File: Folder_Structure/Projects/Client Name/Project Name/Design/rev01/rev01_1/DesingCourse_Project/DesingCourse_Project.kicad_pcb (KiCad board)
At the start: 2 copper layers, 65 x 56 mm, 4 parts

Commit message: Update 16
Initial component placement done
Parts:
- added C1: 820u, LKMI2501K821MF:RA_LKMI2501K821MF_YMIN, B.Cu at (188.5, 137.0)
- added C10: 100n, Capacitor_SMD:C_0603_1608Metric, F.Cu at (153.7, 163.8)
- added C11: 100n, Capacitor_SMD:C_0603_1608Metric, F.Cu at (155.2, 163.8)
- added C12: 100n, Capacitor_SMD:C_0603_1608Metric, F.Cu at (158.2, 177.8)
- added C13: 100n, Capacitor_SMD:C_0603_1608Metric, F.Cu at (168.2, 175.8)
- added C14: 10p, Capacitor_SMD:C_0603_1608Metric, F.Cu at (147.2, 163.8)
- added C15: 10p, Capacitor_SMD:C_0603_1608Metric, F.Cu at (147.2, 171.8)
- added C16: 100n, Capacitor_SMD:C_0603_1608Metric, F.Cu at (168.2, 163.8)
- added C17: 100n, Capacitor_SMD:C_0603_1608Metric, F.Cu at (157.7, 162.2)
- added C18: 100n, Capacitor_SMD:C_0603_1608Metric, F.Cu at (154.2, 157.2)
- added C19: 2u2, Capacitor_SMD:C_0603_1608Metric, F.Cu at (166.2, 177.8)
- added C2: 820u, LKMI2501K821MF:RA_LKMI2501K821MF_YMIN, B.Cu at (198.0, 176.1)
- added C20: 2u2, Capacitor_SMD:C_0603_1608Metric, F.Cu at (170.2, 165.2)
- added C21: 100n, Capacitor_SMD:C_0603_1608Metric, F.Cu at (154.7, 171.8)
- added C22: 1u, Capacitor_SMD:C_0603_1608Metric, F.Cu at (153.2, 171.8)
- added C23: 100n, Capacitor_SMD:C_0603_1608Metric, F.Cu at (143.2, 134.7)
- added C24: 10n, Capacitor_SMD:C_0603_1608Metric, F.Cu at (273.6, 155.7)
- added C25: 2u2, Capacitor_SMD:C_0603_1608Metric, F.Cu at (273.6, 158.2)
- added C26: 2u2, Capacitor_SMD:C_0603_1608Metric, F.Cu at (273.6, 160.7)
- added C27: 120p, Capacitor_SMD:C_0603_1608Metric, F.Cu at (273.6, 163.2)
- added C28: 2u2, Capacitor_SMD:C_0603_1608Metric, F.Cu at (273.6, 165.7)
- added C29: 2u2, Capacitor_SMD:C_0603_1608Metric, F.Cu at (273.6, 168.2)
- added C3: 1u, Capacitor_SMD:C_0603_1608Metric, F.Cu at (165.6, 144.6)
- added C30: 22n, Capacitor_SMD:C_0603_1608Metric, F.Cu at (273.6, 170.7)
- added C31: 2u2, Capacitor_SMD:C_0603_1608Metric, F.Cu at (273.6, 173.2)
- added C32: 100n, Capacitor_SMD:C_0603_1608Metric, F.Cu at (277.6, 155.7)
- added C33: 100n, Capacitor_SMD:C_0603_1608Metric, F.Cu at (277.6, 158.2)
- added C34: 100n, Capacitor_SMD:C_0603_1608Metric, F.Cu at (277.6, 160.7)
- added C35: 100n, Capacitor_SMD:C_0603_1608Metric, F.Cu at (303.3, 157.2)
- added C36: 1u, Capacitor_SMD:C_0603_1608Metric, F.Cu at (277.6, 165.7)
- added C37: 1u, Capacitor_SMD:C_0603_1608Metric, F.Cu at (277.6, 168.2)
- added C38: 1u, Capacitor_SMD:C_0603_1608Metric, F.Cu at (277.6, 170.7)
- added C39: 10u, Capacitor_SMD:C_0603_1608Metric, F.Cu at (277.6, 173.2)
- added C4: 1u, Capacitor_SMD:C_0603_1608Metric, F.Cu at (167.1, 144.6)
- added C40: 1u, Capacitor_SMD:C_0603_1608Metric, F.Cu at (281.6, 155.7)
- added C41: 1u, Capacitor_SMD:C_0603_1608Metric, F.Cu at (281.6, 158.2)
- added C42: 10u, Capacitor_SMD:C_0603_1608Metric, F.Cu at (281.6, 160.7)
- added C43: 1u, Capacitor_SMD:C_0603_1608Metric, F.Cu at (281.6, 163.2)
- added C44: 10u, Capacitor_SMD:C_0603_1608Metric, F.Cu at (281.6, 165.7)
- added C45: 100n, Capacitor_SMD:C_0603_1608Metric, F.Cu at (281.6, 168.2)
- added C46: 100n, Capacitor_SMD:C_0603_1608Metric, F.Cu at (281.6, 170.7)
- added C47: 100n, Capacitor_SMD:C_0603_1608Metric, F.Cu at (281.6, 173.2)
- added C48: 2n2, Capacitor_SMD:C_0603_1608Metric, F.Cu at (189.5, 148.7)
- added C49: 2n2, Capacitor_SMD:C_0603_1608Metric, F.Cu at (189.5, 164.7)
- added C5: 1u, Capacitor_SMD:C_0603_1608Metric, F.Cu at (178.1, 142.1)
- added C50: 2u2, Capacitor_SMD:C_0603_1608Metric, F.Cu at (166.1, 149.2)
- added C51: 51p, Capacitor_SMD:C_0603_1608Metric, F.Cu at (144.1, 152.2)
- added C52: 51p, Capacitor_SMD:C_0603_1608Metric, F.Cu at (144.1, 146.2)
- added C53: 4n7, Capacitor_SMD:C_0603_1608Metric, F.Cu at (158.5, 186.5)
- added C54: 4n7, Capacitor_SMD:C_0603_1608Metric, F.Cu at (162.0, 186.5)
- added C55: 4n7, Capacitor_SMD:C_0603_1608Metric, F.Cu at (165.5, 186.5)
- added C56: 100n, Capacitor_SMD:C_0603_1608Metric, F.Cu at (157.5, 182.5)
- added C57: 100n, Capacitor_SMD:C_0603_1608Metric, F.Cu at (161.0, 182.5)
- added C58: 100n, Capacitor_SMD:C_0603_1608Metric, F.Cu at (166.5, 182.5)
- added C59: 4n7, Capacitor_SMD:C_0603_1608Metric, F.Cu at (154.5, 186.5)
- added C6: 1u, Capacitor_SMD:C_0603_1608Metric, F.Cu at (179.6, 142.1)
- added C60: 100n, Capacitor_SMD:C_0603_1608Metric, F.Cu at (153.5, 182.5)
- added C7: 100n, Capacitor_SMD:C_0603_1608Metric, F.Cu at (212.7, 140.8)
- added C8: 100n, Capacitor_SMD:C_0603_1608Metric, F.Cu at (146.5, 183.6)
- added C9: 10u, Capacitor_SMD:C_0603_1608Metric, F.Cu at (152.2, 163.8)
- added D1: SMAJ60CA, Diode_SMD:D_SMA, F.Cu at (209.2, 137.8)
- added D10: LED_G, Diode_SMD:D_1206_3216Metric, F.Cu at (170.7, 185.2)
- added D11: LED_R, Diode_SMD:D_1206_3216Metric, F.Cu at (173.2, 185.2)
- added D12: BAT60A, Diode_SMD:D_SOD-323, F.Cu at (162.5, 135.4)
- added D13: PMEG6020AELR, Diode_SMD:Nexperia_CFP3_SOD-123W, F.Cu at (274.4, 176.1)
- added D14: BAT60A, Diode_SMD:D_SOD-323, F.Cu at (279.4, 176.0)
- added D15: ESDCAN24-2BLY, ESDCAN24-2BLY:SOT95P237X112-3N, F.Cu at (138.1, 149.2)
- added D2: LED_G, Diode_SMD:D_1206_3216Metric, F.Cu at (215.2, 132.8)
- added D3: LED_G, Diode_SMD:D_1206_3216Metric, F.Cu at (162.1, 142.1)
- added D4: BAT60A, Diode_SMD:D_SOD-323, F.Cu at (182.0, 142.9)
- added D5: LED_G, Diode_SMD:D_1206_3216Metric, F.Cu at (183.1, 139.1)
- added D6: PESD3V3U1UA,115, PESD3V3U1UA_115:DIO_PESD3V3U1UA_115, F.Cu at (137.6, 164.5)
- added D7: BAT60A, Diode_SMD:D_SOD-323, F.Cu at (141.6, 164.5)
- added D8: SMAJ5.0A, Diode_SMD:D_SMA, F.Cu at (137.6, 159.5)
- added D9: BAT60A, Diode_SMD:D_SOD-323, F.Cu at (141.6, 161.5)
- added FB1: 120R, BLM18PG121SN1D:BEADC1608X95N, F.Cu at (151.7, 171.8)
- added FID1: 1mm/circular, Fiducial:Fiducial_1mm_Mask2mm, F.Cu at (130.0, 133.2)
- added FID2: 1mm/circular, Fiducial:Fiducial_1mm_Mask2mm, F.Cu at (220.0, 133.2)
- added FID3: 1mm/circular, Fiducial:Fiducial_1mm_Mask2mm, F.Cu at (220.0, 188.2)
- added ID1: ~, JGB_Library:hot-surface, F.Cu at (341.3, 68.6)
- added ID2: ~, JGB_Library:high-voltage, F.Cu at (323.8, 83.9)
- added ID3: ~, JGB_Library:ESD-suceptible, F.Cu at (326.1, 69.3)
- added ID4: ~, JGB_Library:IC-logo, F.Cu at (352.8, 80.9)
- added ID5: ~, JGB_Library:4_Layer_ID, F.Cu at (198.2, 197.6)
- added ID6: ~, JGB_Library:Project_ID, F.Cu at (334.4, 98.3)
- added J1: XT60PW-M, XT60PW-M:AMASS_XT60PW-M, F.Cu at (199.0, 134.2)
- added J10: 874380443, 874380843:MOLEX_874380443, F.Cu at (130.1, 149.2)
- added J11: 874380643, 874380843:MOLEX_874380643, F.Cu at (160.5, 193.0)
- added J2: TYPE-C-31-M-12, TYPE-C-31-M-12:HRO_TYPE-C-31-M-12, F.Cu at (178.4, 125.3)
- added J3: 874380243, 874380843:MOLEX_874380243, F.Cu at (146.7, 193.2)
- added J4: 874380843, 874380843:MOLEX_874380843, F.Cu at (130.1, 168.0)
- added J5: 874380343, 874380843:MOLEX_874380343, F.Cu at (143.2, 128.2)
- added J6: 874380643, 874380843:MOLEX_874380643, F.Cu at (157.5, 128.4)
- added J7: 7461084, WP-BUTR:WP-BUTR_7461084, F.Cu at (218.8, 149.2)
- added J8: 7461084, WP-BUTR:WP-BUTR_7461084, F.Cu at (218.8, 165.2)
- added J9: 7461084, WP-BUTR:WP-BUTR_7461084, F.Cu at (218.8, 181.2)
- added L1: 22u, L_Bourns_SDR0805:IND_BOURNS_SDR0805, F.Cu at (298.3, 148.8)
- added L2: 744227S, WE-SL2:WE-SL2, F.Cu at (151.1, 149.2)
- added NT1: NetTie_2, NetTie:NetTie-2_SMD_Pad0.5mm, F.Cu at (278.5, 178.2)
- added NT2: NetTie_2, NetTie:NetTie-2_SMD_Pad0.5mm, F.Cu at (210.8, 149.7)
- added NT3: NetTie_2, NetTie:NetTie-2_SMD_Pad0.5mm, F.Cu at (210.8, 165.7)
- added NT4: NetTie_2, NetTie:NetTie-2_SMD_Pad0.5mm, F.Cu at (210.8, 181.7)
- added NT5: NetTie_2, NetTie:NetTie-2_SMD_Pad0.5mm, F.Cu at (203.3, 183.2)
- added Q1: HSBA15810C, Package_SO:HSBA15810C, F.Cu at (208.8, 146.2)
- added Q2: HSBA15810C, Package_SO:HSBA15810C, F.Cu at (208.8, 153.2)
- added Q3: HSBA15810C, Package_SO:HSBA15810C, F.Cu at (208.8, 162.2)
- added Q4: HSBA15810C, Package_SO:HSBA15810C, F.Cu at (208.8, 169.2)
- added Q5: HSBA15810C, Package_SO:HSBA15810C, F.Cu at (208.8, 178.2)
- added Q6: HSBA15810C, Package_SO:HSBA15810C, F.Cu at (208.8, 185.1)
- added R1: 39k, Resistor_SMD:R_0603_1608Metric, F.Cu at (211.2, 132.8)
- added R10: 1k, Resistor_SMD:R_0603_1608Metric, F.Cu at (184.6, 142.1)
- added R11: 39k, Resistor_SMD:R_0603_1608Metric, F.Cu at (212.7, 137.4)
- added R12: 2k2, Resistor_SMD:R_0603_1608Metric, F.Cu at (214.2, 140.8)
- added R13: 2k2, Resistor_SMD:R_0603_1608Metric, F.Cu at (146.5, 185.1)
- added R14: 2k2, Resistor_SMD:R_0603_1608Metric, F.Cu at (144.2, 157.2)
- added R15: 0R, Resistor_SMD:R_0603_1608Metric, F.Cu at (151.7, 166.8)
- added R16: 0R, Resistor_SMD:R_0603_1608Metric, F.Cu at (151.7, 169.3)
- added R17: 1k, Resistor_SMD:R_0603_1608Metric, F.Cu at (170.7, 181.2)
- added R18: 1k, Resistor_SMD:R_0603_1608Metric, F.Cu at (173.2, 181.2)
- added R19: 0R, Resistor_SMD:R_0603_1608Metric, F.Cu at (160.7, 160.8)
- added R2: 0R, Resistor_SMD:R_0603_1608Metric, F.Cu at (173.9, 132.8)
- added R20: 2k2, Resistor_SMD:R_0603_1608Metric, F.Cu at (141.7, 134.7)
- added R21: 16k, Resistor_SMD:R_0603_1608Metric, F.Cu at (285.7, 155.7)
- added R22: 205k, Resistor_SMD:R_0603_1608Metric, F.Cu at (285.7, 158.2)
- added R23: 10k, Resistor_SMD:R_0603_1608Metric, F.Cu at (285.7, 160.7)
- added R24: 10k, Resistor_SMD:R_0603_1608Metric, F.Cu at (285.7, 163.2)
- added R25: 1M, Resistor_SMD:R_0603_1608Metric, F.Cu at (285.7, 165.7)
- added R26: 18k, Resistor_SMD:R_0603_1608Metric, F.Cu at (285.7, 168.2)
- added R27: 3k3, Resistor_SMD:R_0603_1608Metric, F.Cu at (285.7, 170.7)
- added R28: 39k, Resistor_SMD:R_0603_1608Metric, F.Cu at (285.7, 173.2)
- added R29: 2k2, Resistor_SMD:R_0603_1608Metric, F.Cu at (289.7, 155.7)
- added R3: 0R, Resistor_SMD:R_0603_1608Metric, F.Cu at (172.4, 132.8)
- added R30: 39k, Resistor_SMD:R_0603_1608Metric, F.Cu at (289.7, 158.2)
- added R31: 2k2, Resistor_SMD:R_0603_1608Metric, F.Cu at (289.7, 160.7)
- added R32: 39k, Resistor_SMD:R_0603_1608Metric, F.Cu at (289.7, 163.2)
- added R33: 2k2, Resistor_SMD:R_0603_1608Metric, F.Cu at (289.7, 165.7)
- added R34: 4R7, Resistor_SMD:R_0603_1608Metric, F.Cu at (210.1, 142.5)
- added R35: 4R7, Resistor_SMD:R_0603_1608Metric, F.Cu at (202.8, 154.2)
- added R36: 39k, Resistor_SMD:R_0603_1608Metric, F.Cu at (204.3, 154.2)
- added R37: 100R, Resistor_SMD:R_0603_1608Metric, F.Cu at (191.8, 149.4)
- added R38: 100R, Resistor_SMD:R_0603_1608Metric, F.Cu at (191.8, 147.9)
- added R39: 1m, RES_WSLP2726L5000FEA:WSLP2726_1mOHM_VIS, F.Cu at (197.8, 148.7)
- added R4: 0R, Resistor_SMD:R_0603_1608Metric, F.Cu at (175.5, 135.8)
- added R40: 4R7, Resistor_SMD:R_0603_1608Metric, F.Cu at (210.8, 158.2)
- added R41: 4R7, Resistor_SMD:R_0603_1608Metric, F.Cu at (202.8, 170.2)
- added R42: 39k, Resistor_SMD:R_0603_1608Metric, F.Cu at (204.3, 170.2)
- added R43: 100R, Resistor_SMD:R_0603_1608Metric, F.Cu at (191.8, 165.4)
- added R44: 100R, Resistor_SMD:R_0603_1608Metric, F.Cu at (191.8, 163.9)
- added R45: 1m, RES_WSLP2726L5000FEA:WSLP2726_1mOHM_VIS, F.Cu at (197.8, 164.7)
- added R46: 4R7, Resistor_SMD:R_0603_1608Metric, F.Cu at (210.8, 174.2)
- added R47: 4R7, Resistor_SMD:R_0603_1608Metric, F.Cu at (202.8, 186.2)
- added R48: 39k, Resistor_SMD:R_0603_1608Metric, F.Cu at (204.3, 186.2)
- added R49: 10k, Resistor_SMD:R_0603_1608Metric, F.Cu at (159.6, 152.8)
- added R5: 5k1, Resistor_SMD:R_0603_1608Metric, F.Cu at (178.5, 135.8)
- added R50: 10R, Resistor_SMD:R_0603_1608Metric, F.Cu at (144.1, 147.8)
- added R51: 10R, Resistor_SMD:R_0603_1608Metric, F.Cu at (144.1, 150.8)
- added R52: 120R, Resistor_SMD:R_0603_1608Metric, F.Cu at (141.6, 149.2)
- added R53: 2k2, Resistor_SMD:R_0603_1608Metric, F.Cu at (158.5, 185.0)
- added R54: 2k2, Resistor_SMD:R_0603_1608Metric, F.Cu at (162.0, 185.0)
- added R55: 2k2, Resistor_SMD:R_0603_1608Metric, F.Cu at (165.5, 185.0)
- added R56: 10k, Resistor_SMD:R_0603_1608Metric, F.Cu at (159.0, 182.5)
- added R57: 10k, Resistor_SMD:R_0603_1608Metric, F.Cu at (162.5, 182.5)
- added R58: 10k, Resistor_SMD:R_0603_1608Metric, F.Cu at (165.0, 182.5)
- added R59: 10k, Resistor_SMD:R_0603_1608Metric, F.Cu at (154.5, 185.0)
- added R6: 5k1, Resistor_SMD:R_0603_1608Metric, F.Cu at (177.0, 135.8)
- added R60: 0R, Resistor_SMD:R_0603_1608Metric, F.Cu at (155.0, 182.5)
- added R61: 0R, Resistor_SMD:R_0603_1608Metric, F.Cu at (136.1, 128.5)
- added R62: 0R, Resistor_SMD:R_0603_1608Metric, F.Cu at (215.0, 128.2)
- added R63: 0R, Resistor_SMD:R_0603_1608Metric, F.Cu at (212.5, 193.8)
- added R64: 0R, Resistor_SMD:R_0603_1608Metric, F.Cu at (137.5, 193.2)
- added R7: 22R, Resistor_SMD:R_0603_1608Metric, F.Cu at (181.0, 135.8)
- added R8: 22R, Resistor_SMD:R_0603_1608Metric, F.Cu at (182.5, 135.8)
- added R9: 1k, Resistor_SMD:R_0603_1608Metric, F.Cu at (163.1, 145.4)
- added SW1: ~, PTS526SK15SMTR2LFS:SMT_FS, F.Cu at (149.2, 157.2)
- added TH1: 10k, Resistor_SMD:R_0603_1608Metric, F.Cu at (146.5, 187.1)
- added U1: PUSB3AB6Z, PUSB3AB6Z:IC_PUSB3AB6Z, F.Cu at (178.0, 132.8)
- added U2: AMS1117-3.3, Package_TO_SOT_SMD:SOT-223-3_TabPin2, F.Cu at (172.2, 143.0)
- added U3: STM32F405RGTx, Package_QFP:LQFP-64_10x10mm_P0.5mm, F.Cu at (162.2, 169.8)
- added U4: DRV8302DCA, DRV8302DCA:SOP50P810X120-57N, F.Cu at (297.3, 162.2)
- added U5: SN65HVD230D, SN65HVD230D:SOIC127P599X175-8N, F.Cu at (161.6, 149.2)
- added Y1: 8MHz, X50328MSB2GI:XTAL_MSB2GI_YXC, F.Cu at (148.2, 167.8)
- MH1, MH2, MH3, MH4: value MountingHole_2.7mm_M2.5 -> M3; footprint MountingHole:MountingHole_2.7mm_M2.5 -> MountingHole:MountingHole_3mm_Pad_Via
- moved MH3 57.8 mm to (130.0, 193.2)
- moved MH1 55.5 mm to (130.0, 128.2)
- moved MH4 27.9 mm to (220.0, 193.2)
- moved MH2 24.1 mm to (220.0, 128.2)
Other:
- board size 65 x 56 mm -> 100 x 75 mm
- copper layers 2 -> 4
- board text added: "CAN"
- board text added: "COM"
- board text added: "FILTERS"
- board text added: "INPUT"
- board text added: "OUTPUT"
- board text added: "PROG"
- board text added: "SENSOR"
- board text added: "SERVO"
- board text added: "USB"
- board text removed: "Extend PCB edge 0.5mm if using SMT header"

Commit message: Update17
Design rules and stack defined.

Check againg DR and proceed with layout.
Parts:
- C39, C42, C44: footprint Capacitor_SMD:C_0603_1608Metric -> Capacitor_SMD:C_1210_3225Metric
- C45, C46, C47, C48, C49, R37, R38, R43, R44: moved to B.Cu
- moved R26 113.7 mm to (172.1, 162.7), turned to -90 degrees
- moved U4 113.7 mm to (184.2, 173.4)
- moved L1 113.3 mm to (185.4, 158.4), turned to 180 degrees
- moved C35 112.9 mm to (190.9, 167.9)
- moved R27 112.3 mm to (173.6, 162.7), turned to 90 degrees
- moved D14 110.6 mm to (170.1, 158.9), turned to -90 degrees
- moved R21 110.0 mm to (176.4, 168.2)
- moved R23 109.7 mm to (176.4, 169.9)
- moved R24 109.6 mm to (176.4, 171.7)
- moved R22 109.5 mm to (176.4, 164.9)
- moved C44 109.0 mm to (172.9, 158.4), turned to 90 degrees
- moved C42 105.5 mm to (176.1, 158.4), turned to 90 degrees
- moved NT1 104.5 mm to (174.0, 174.9)
- moved R62 103.1 mm to (135.0, 193.2), turned to 0 degrees
- moved C40 101.4 mm to (180.6, 164.4), turned to 90 degrees
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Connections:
- net Net-(C24-Pad1) renamed /MOSFET_DRIVER/Node8
- net Net-(D10-A) renamed /MCU/Node5
- net Net-(D11-A) renamed /MCU/Node6
- net Net-(D2-A) renamed /INPUT/Node1
- net Net-(D3-A) renamed /STEP_DOWN/Node2
- net Net-(D5-A) renamed /STEP_DOWN/Node3
- net Net-(J2-SHIELD-PadS1) renamed /USB-C/Shield_USB
- net Net-(J5-3-Pad3_1) renamed /MCU/Node7
- net Net-(MH1-Pad1) renamed /MECHANICAL/Node10
- net Net-(MH2-Pad1) renamed /MECHANICAL/Node11
- net Net-(MH3-Pad1) renamed /MECHANICAL/Node12
- net Net-(MH4-Pad1) renamed /MECHANICAL/Node13
- net Net-(R14-Pad1) renamed /MCU/Node4
- net Net-(U4-AVDD) renamed /MOSFET_DRIVER/<NO NET>
- net Net-(U5-RS) renamed /CAN/CAN_RS
- D15 pad 1: /CAN/CONN_CAN_P -> /CAN/CONN_CAN_N
- D15 pad 2: /CAN/CONN_CAN_N -> /CAN/CONN_CAN_P
- J10 pad 1_1: P5V -> GND
- J10 pad 1_2: P5V -> GND
- J10 pad 2_1: /CAN/CONN_CAN_P -> /CAN/CONN_CAN_N
- J10 pad 2_2: /CAN/CONN_CAN_P -> /CAN/CONN_CAN_N
- J10 pad 3_1: /CAN/CONN_CAN_N -> /CAN/CONN_CAN_P
- J10 pad 3_2: /CAN/CONN_CAN_N -> /CAN/CONN_CAN_P
- J10 pad 4_1: GND -> P5V
- J10 pad 4_2: GND -> P5V
- L2 pad 1: /CAN/R_CAN_P -> /CAN/R_CAN_N
- L2 pad 2: /CAN/R_CAN_N -> /CAN/R_CAN_P
- L2 pad 3: /CAN/CAN_N -> /CAN/CAN_P
- L2 pad 4: /CAN/CAN_P -> /CAN/CAN_N
- U1 pad 3: /USB-C/P5V-C -> VBUS
- U1 pad 5: /USB-C/P5V-C -> VBUS
- U3 pad 14: SENS3 -> SENS1
- U3 pad 16: SENS1 -> SENS3

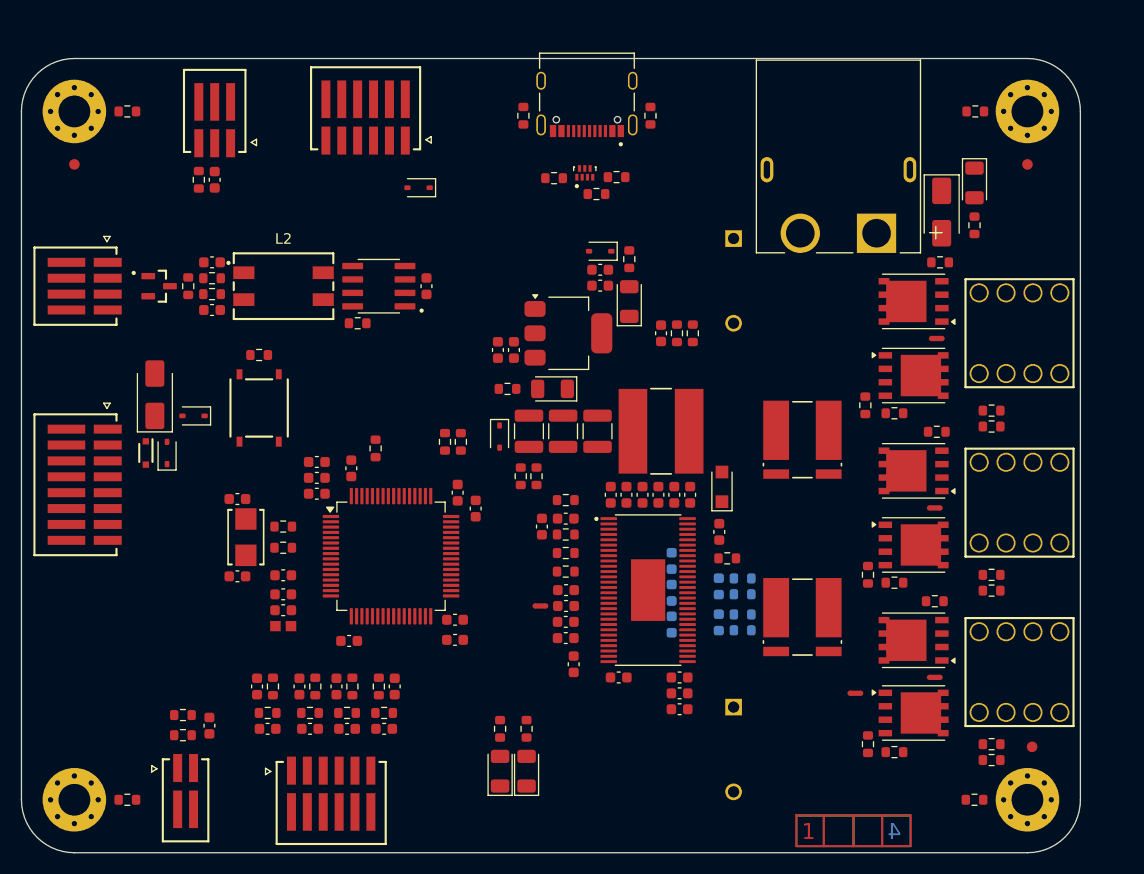
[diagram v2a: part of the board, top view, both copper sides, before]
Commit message: Update18
Layout finished, clean up or layout and designators.
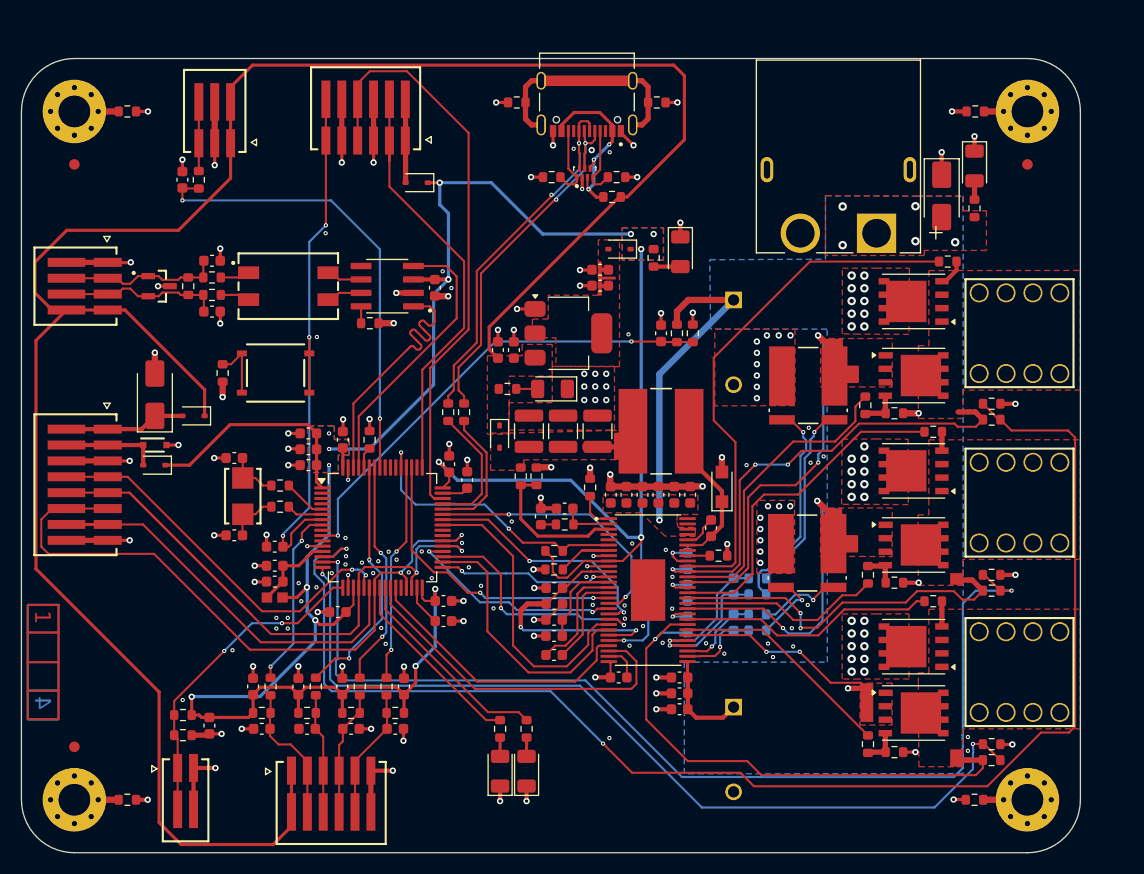
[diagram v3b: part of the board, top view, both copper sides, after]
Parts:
- moved FID3 90.4 mm to (130.0, 188.2)
- moved ID5 76.1 mm to (125.6, 174.8), turned to -90 degrees
- moved NT4 8.31 mm to (214.1, 189.5), turned to 180 degrees
- moved NT2 7.38 mm to (213.9, 156.6), turned to 180 degrees
- moved NT3 7.32 mm to (213.9, 172.5), turned to 180 degrees
- moved D5 6.74 mm to (187.2, 141.5), turned to -90 degrees
- moved R45 6.07 mm to (199.2, 169.9)
- moved C1 5.80 mm to (192.2, 146.0)
- moved R39 5.15 mm to (199.3, 154.1)
- moved C14 3.89 mm to (145.1, 161.0)
- moved C15 3.89 mm to (145.1, 168.3)
- moved R15 3.89 mm to (149.4, 163.6)
- moved R16 3.89 mm to (149.4, 165.6)
- moved Y1 3.89 mm to (145.9, 164.6)
- moved R14 3.84 mm to (144.0, 152.9), turned to -90 degrees
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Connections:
- net /MOSFET_DRIVER/<NO NET> renamed /MOSFET_DRIVER/Node9
- net Net-(D4-A) renamed /STEP_DOWN/P3V3_I
- R56 pad 2: HALL1_OUT -> HALL_1_OUT
- R57 pad 2: HALL2_OUT -> HALL_2_OUT
- R58 pad 2: HALL3_OUT -> HALL_3_OUT
- U3 pad 26: BR_SD2 -> BR_SO2
- U3 pad 27: BR_SD1 -> BR_SO1
- U3 pad 52: /MCU/HALL3_OUT -> HALL_3_OUT
- U3 pad 58: /MCU/HALL1_OUT -> HALL_2_OUT
- U3 pad 59: /MCU/HALL2_OUT -> HALL_1_OUT
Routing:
- net P3V3: track 0.00 -> 244.9 mm, vias 0 -> 16
- net P5V: track 0.00 -> 208.5 mm
- net GND: track 0.00 -> 164.3 mm, vias 0 -> 178
- net SENS1: track 0.00 -> 132.7 mm, vias 0 -> 2
- net SENS2: track 0.00 -> 99.7 mm, vias 0 -> 2
- net SENS3: track 0.00 -> 83.8 mm, vias 0 -> 2
- net /MCU/RX_SDA_NSS: track 0.00 -> 71.2 mm, vias 0 -> 2
- net /MCU/TX_SCL_MOSI: track 0.00 -> 64.8 mm, vias 0 -> 2
- net /MCU/SWDIO: track 0.00 -> 55.8 mm
- net /MCU/NRST: track 0.00 -> 54.6 mm, vias 0 -> 3
- net H3_VS: track 0.00 -> 51.6 mm, vias 0 -> 1
- net M_H1: track 0.00 -> 49.9 mm
- net /MCU/AN_IN: track 0.00 -> 44.6 mm, vias 0 -> 2
- net /MCU/SERVO: track 0.00 -> 43.9 mm, vias 0 -> 2
- net H1_VS: track 0.00 -> 43.3 mm, vias 0 -> 3
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- added copper zone on B.Cu, net +VDC
- added copper zone on F.Cu, net +VDC
- added copper zone on F.Cu, net /MOSFET/PHASE_1
- added copper zone on F.Cu, net /MOSFET/PHASE_2
- added copper zone on F.Cu, net /MOSFET/PHASE_3
- added copper zone on F.Cu, net /MOSFET_DRIVER/P5V_DRV
- added copper zone on F.Cu, net /STEP_DOWN/P3V3_I
- added copper zone on F.Cu, net GND
- added copper zone on In1.Cu, net GND
- added copper zone on In2.Cu, net GND
- added copper zone on F.Cu, net H1_LOW
- added copper zone on F.Cu, net H2_LOW
- added copper zone on F.Cu, net H3_LOW
- added copper zone on B.Cu, net P3V3
- added copper zone on F.Cu, net P3V3
- added copper zone on F.Cu, net P5V

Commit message: Update19
PCB finished before applying curved traces
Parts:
- C14, ID4, ID6: moved to B.Cu
- moved ID4 206.0 mm to (153.0, 130.8), turned to 180 degrees
- moved ID3 188.8 mm to (181.2, 190.3)
- moved ID6 181.8 mm to (160.0, 149.7), turned to 180 degrees
- moved ID2 144.4 mm to (188.4, 134.2)
- moved ID1 143.1 mm to (200.0, 190.4)
- moved D10 2.58 mm to (167.6, 190.5)
- moved D11 2.58 mm to (170.1, 190.5)
- moved R17 2.58 mm to (167.6, 186.5)
- moved R18 2.58 mm to (170.1, 186.5)
- moved C23 1.93 mm to (138.2, 134.7)
- moved R20 1.93 mm to (139.8, 134.7)
- moved R4 0.05 mm to (180.7, 136.3)
- moved R5 0.05 mm to (181.1, 134.4)
- moved R6 0.05 mm to (175.0, 134.4)
- moved U1 0.05 mm to (178.1, 134.1)
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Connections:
- net CAN_RX renamed CAN_TXRX_N
- net CAN_TX renamed CAN_TXRX_P
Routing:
- net /USB-C/USB-C_N: track 35.5 -> 38.5 mm
- net /MCU/LED_RED: track 19.7 -> 17.1 mm
- net H1: track 25.4 -> 23.3 mm
- net /MCU/SERVO: track 43.9 -> 45.8 mm
- net /MCU/LED_GREEN: track 18.0 -> 16.1 mm
- net /MCU/Node7: track 6.53 -> 7.80 mm
- net /USB-C/USB-C_P: track 37.1 -> 37.8 mm
- net /USB-C/CC2: track 7.05 -> 7.58 mm
- net GND: vias 178 -> 185
- added copper zone on B.Cu, net GND
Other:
- board text added: "*"
- board text added: "+VDC"
- board text added: "+VDC - ON"
- board text added: "0.03 mm"
- board text added: "0.07 mm"
- board text added: "0.1200 mm / 0.2000 mm"
- board text added: "0.203 mm"
- board text added: "1.03 mm"
- board text added: "1.6560 mm"
- board text added: "100.0000 mm x 75.0000 mm"
- board text added: "4"
- board text added: "4.6"
- board text added: "BOT_SGN.Cu"
- board text added: "Blue"
- board text added: "COMM"
- board text added: "D15"
- board text added: "D6"
- board text added: "Dielectric 1"
- board text added: "Dielectric 2"
- board text added: "Dielectric 3"
- board text added: "FB1"
- board text added: "GND"
- board text added: "GND CAN_N CAN_P P5V"
- board text added: "GREEN LED"
- board text added: "H1"
- board text added: "H2"
- board text added: "H3"
- board text added: "HAL lead-free"
- board text added: "J1"
- board text added: "J10"
- board text added: "J11"
- board text added: "J2"
- board text added: "J3"
- board text added: "J4"
- board text added: "J5"
- board text added: "J6"
- board text added: "J7"
- board text added: "J8"
- board text added: "J9"
- board text added: "L2"
- board text added: "L2_GND.Cu"
- board text added: "L3_GND.Cu"
- board text added: "NRST GND SWDIO GND SWCLK P3V3"
- board text added: "P3V3 - ON"
- board text added: "P5V"
- board text added: "P5V - ON"
- board text added: "P5V P3V3 GND SCK_ADC_EXT RX_SDA_NSS TX_SCL_MOSI MISO_ADC_EXT2 GND"
- board text added: "RED LED"
- board text added: "T1"
- board text added: "TEMP & HALL SENSOR"
- board text added: "THERMISTOR"
- board text added: "TOP_SGN.Cu"
- board text added: "U1"
- board text added: "U4"
- board text added: "U5"
- board text added: "USB-C"
- board text added: "White"
- board text added: "Yes"
- board text added: "prepreg"
- board text removed: "0.035 mm"
- board text removed: "0.2000 mm / 0.0000 mm"
- board text removed: "1.51 mm"
- board text removed: "1.6000 mm"
- board text removed: "2"
- board text removed: "4.5"
- board text removed: "65.1000 mm x 56.1000 mm"
- board text removed: "B.Cu"
- board text removed: "Dielectric"
- board text removed: "F.Cu"
- board text removed: "Green"
- board text removed: "None"

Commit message: Update20
DRC "clear".

Create gerber files
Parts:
- C14: moved to F.Cu
- moved D1 0.72 mm to (211.9, 135.5)
- moved NT5 0.50 mm to (204.2, 183.2)
- turned C14 to 180 degrees
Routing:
- net /MCU/RX_SDA_NSS: track 71.2 -> 54.4 mm
- net /MCU/SWCLK: track 41.3 -> 38.3 mm
- net GND: track 164.3 -> 167.2 mm, vias 185 -> 524
- net /MOSFET_DRIVER/DTC: track 7.54 -> 5.10 mm
- net /MOSFET/SH1_P: track 21.1 -> 19.0 mm
- net H2_VS: track 33.8 -> 35.9 mm, vias 2 -> 3
- net SENS1: track 132.7 -> 130.7 mm
- net P5V: track 208.5 -> 206.7 mm
- net P3V3: track 244.9 -> 243.1 mm
- net H3_VS: track 51.6 -> 50.0 mm
- net /MCU/TX_SCL_MOSI: track 64.8 -> 63.1 mm
- net SENS3: track 83.8 -> 82.6 mm
- net H1_VS: track 43.3 -> 42.2 mm
- net H3: track 28.5 -> 27.4 mm
- net /MCU/SWDIO: track 55.9 -> 54.8 mm
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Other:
- board text added: "0.2000 mm"
- board text added: "BOTTOM ASSEMBLY"
- board text added: "TOP ASSEMBLY"
- board text removed: "0.3000 mm"

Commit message: Update21
Save before created manuf and assy files
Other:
- board text removed: "COM"
- board text removed: "INPUT"
- board text removed: "USB"
